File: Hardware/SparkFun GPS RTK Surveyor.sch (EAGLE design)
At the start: 101 parts, among them J16 microSD, J17 Qwiic Right Angle, J3 USB Female Type C Connector, J4 Qwiic Right Angle, J5 USB Female Type C Connector, J6 Start Base, J7 Power Switch, Q2 MBT3904DW1T1, U10 MCP73833, U2 3.3V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

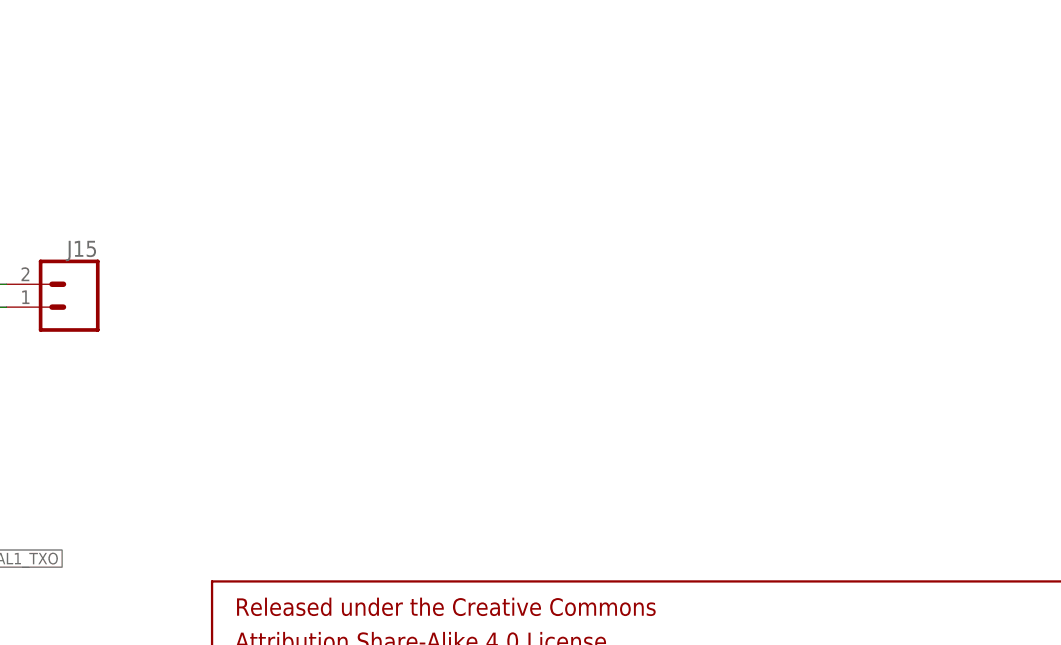
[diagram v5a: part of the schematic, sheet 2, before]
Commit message: Add slide switch to optionally route PPS to Data port
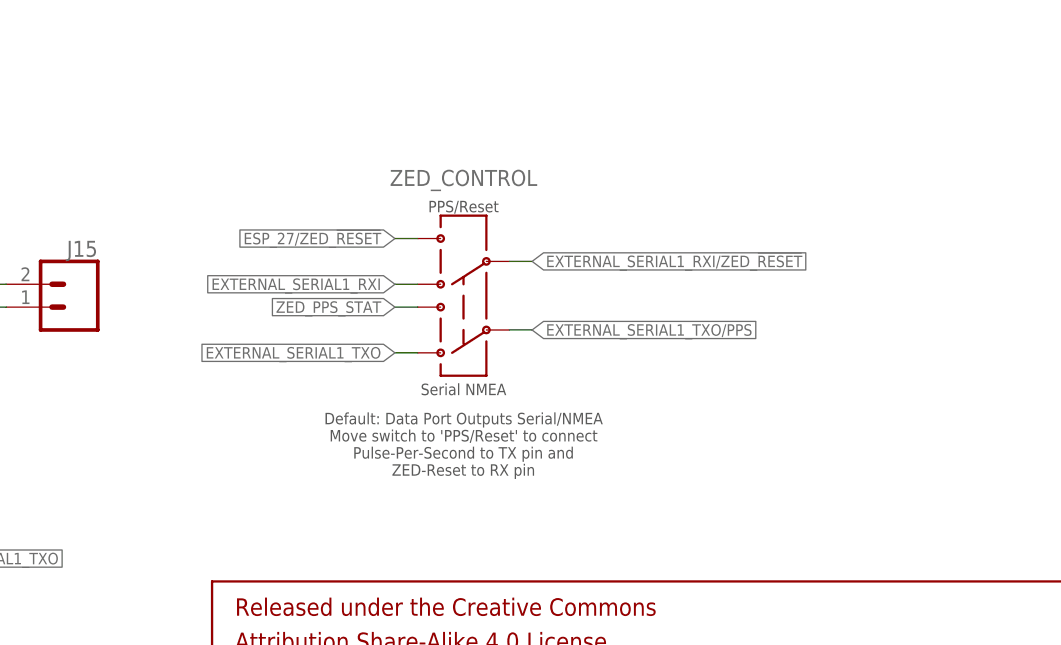
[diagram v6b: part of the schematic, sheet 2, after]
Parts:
- added ZED_CONTROL: (no value), SparkFun-Switches:SWITCH-DPDT-SMD-AYZ0202
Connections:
- new net EXTERNAL_SERIAL1_RXI/ZED_!RESET!: J12.2, J2.3, ZED_CONTROL.5
- new net EXTERNAL_SERIAL1_TXO/PPS: J12.3, J2.2, ZED_CONTROL.2
- net ESP_27/ZED_!RESET!: now also ZED_CONTROL.4
- net EXTERNAL_SERIAL1_RXI: now also ZED_CONTROL.6; no longer J12.2, J2.3
- net EXTERNAL_SERIAL1_TXO: now also ZED_CONTROL.3; no longer J12.3, J2.2
- net ZED_PPS_STAT: now also ZED_CONTROL.1
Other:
- note added: "Default: Data Port Outputs Serial/NMEA Move switch to 'PPS/Reset' to connect Pulse-Per-Second to TX pin and ZED-Reset to RX pin"
- note added: "PPS/Reset"
- note added: "Serial NMEA"

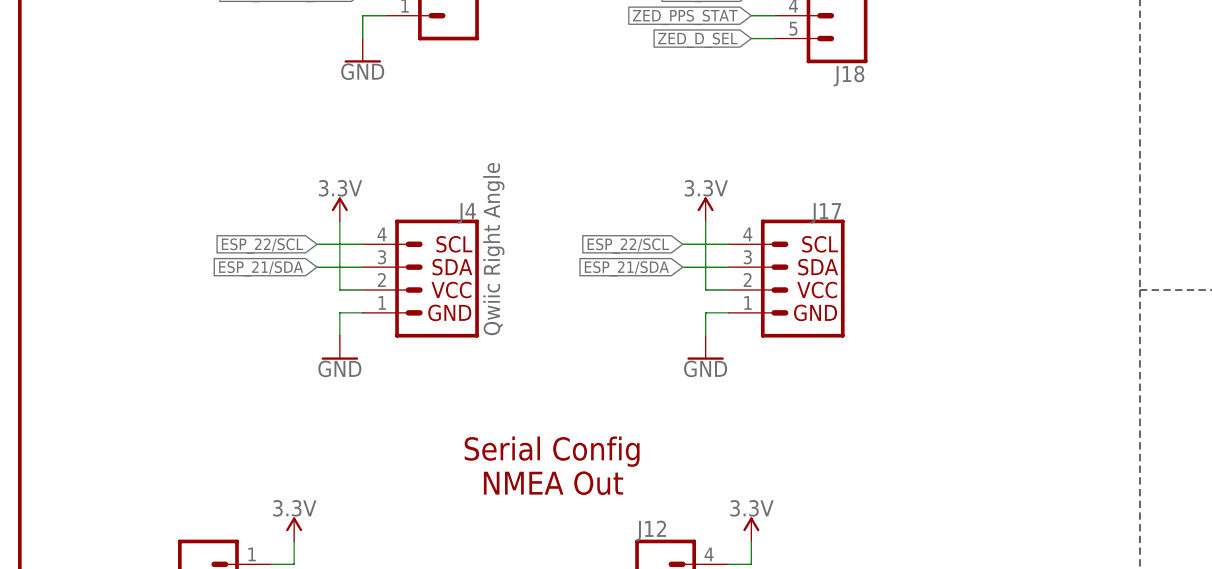
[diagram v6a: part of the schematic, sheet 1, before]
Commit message: Add internal Qwiic connector
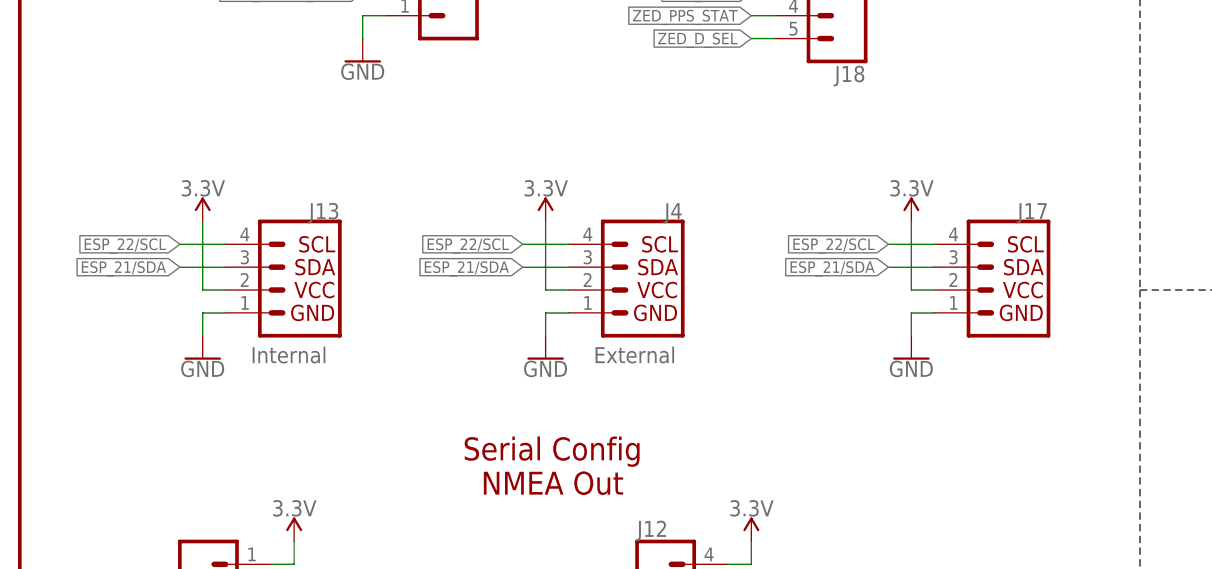
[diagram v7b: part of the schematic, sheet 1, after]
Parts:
- added J13: Internal, SparkFun-Connectors:I2C_STANDARDQWIIC
- J4: value Qwiic Right Angle -> External
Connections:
- net 3.3V: now also J13.2
- net ESP_21/SDA: now also J13.3
- net ESP_22/SCL: now also J13.4
- net GND: now also J13.1
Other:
- moved on the sheet: J17, J4
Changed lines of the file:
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@@
 <part name="JP61" library="SparkFun-Aesthetics" deviceset="FIDUCIAL" device="UFIDUCIAL" value="FIDUCIALUFIDUCIAL"/>
 <part name="SUPPLY8" library="SparkFun-PowerSymbols" deviceset="3.3V" device=""/>
-<part name="J4" library="SparkFun-Connectors" deviceset="I2C_STANDARD" device="QWIIC" value="Qwiic Right Angle"/>
+<part name="J4" library="SparkFun-Connectors" deviceset="I2C_STANDARD" device="QWIIC" value="External"/>
 <part name="LOGO1" library="SparkFun-Aesthetics" deviceset="OSHW-LOGO" device="MINI"/>
 <part name="GND3" library="SparkFun-PowerSymbols" deviceset="GND" device=""/>
@@
 <part name="J18" library="SparkFun-Connectors" deviceset="CONN_05" device="NO_SILK"/>
 <part name="ZED_CONTROL" library="SparkFun-Switches" deviceset="SWITCH-DPDT" device="-SMD-AYZ0202"/>
+<part name="SUPPLY29" library="SparkFun-PowerSymbols" deviceset="3.3V" device=""/>
+<part name="J13" library="SparkFun-Connectors" deviceset="I2C_STANDARD" device="QWIIC" value="Internal"/>
+<part name="GND12" library="SparkFun-PowerSymbols" deviceset="GND" device=""/>
 </parts>
 <sheets>
@@
 <instance part="JP21" gate="G$1" x="416.56" y="33.02" smashed="yes" rot="R270"/>
 <instance part="JP61" gate="G$1" x="419.1" y="33.02" smashed="yes"/>
-<instance part="SUPPLY8" gate="G$1" x="35.56" y="127" smashed="yes">
-<attribute name="VALUE" x="35.56" y="129.794" size="1.778" layer="96" align="bottom-center"/>
-</instance>
-<instance part="J4" gate="G$1" x="45.72" y="119.38" smashed="yes" rot="MR0">
-<attribute name="VALUE" x="51.562" y="133.604" size="1.778" layer="96" font="vector" rot="MR270" align="top-left"/>
-<attribute name="NAME" x="50.8" y="127.254" size="1.778" layer="95" font="vector" rot="MR0"/>
+<instance part="SUPPLY8" gate="G$1" x="58.42" y="127" smashed="yes">
+<attribute name="VALUE" x="58.42" y="129.794" size="1.778" layer="96" align="bottom-center"/>
+</instance>
+<instance part="J4" gate="G$1" x="68.58" y="119.38" smashed="yes" rot="MR0">
+<attribute name="VALUE" x="63.754" y="111.252" size="1.778" layer="96" font="vector" rot="MR180" align="top-left"/>
+<attribute name="NAME" x="73.66" y="127.254" size="1.778" layer="95" font="vector" rot="MR0"/>
 </instance>
 <instance part="LOGO1" gate="G$1" x="417.576" y="45.974" smashed="yes"/>
@@
 <attribute name="REV" x="419.1" y="6.604" size="2.7432" layer="94" font="vector"/>
 </instance>
-<instance part="GND1" gate="1" x="35.56" y="111.76" smashed="yes">
-<attribute name="VALUE" x="35.56" y="111.506" size="1.778" layer="96" align="top-center"/>
+<instance part="GND1" gate="1" x="58.42" y="111.76" smashed="yes">
+<attribute name="VALUE" x="58.42" y="111.506" size="1.778" layer="96" align="top-center"/>
 </instance>
 <instance part="GND28" gate="1" x="304.8" y="208.28" smashed="yes">
@@
 <attribute name="VALUE" x="322.58" y="165.354" size="1.778" layer="96" align="bottom-center"/>
 </instance>
-<instance part="J17" gate="G$1" x="86.36" y="119.38" smashed="yes" rot="MR0">
-<attribute name="NAME" x="91.44" y="127.254" size="1.778" layer="95" font="vector" rot="MR0"/>
-</instance>
-<instance part="GND11" gate="1" x="76.2" y="111.76" smashed="yes">
-<attribute name="VALUE" x="76.2" y="111.506" size="1.778" layer="96" align="top-center"/>
-</instance>
-<instance part="SUPPLY14" gate="G$1" x="76.2" y="127" smashed="yes">
-<attribute name="VALUE" x="76.2" y="129.794" size="1.778" layer="96" align="bottom-center"/>
+<instance part="J17" gate="G$1" x="109.22" y="119.38" smashed="yes" rot="MR0">
+<attribute name="NAME" x="114.3" y="127.254" size="1.778" layer="95" font="vector" rot="MR0"/>
+</instance>
+<instance part="GND11" gate="1" x="99.06" y="111.76" smashed="yes">
+<attribute name="VALUE" x="99.06" y="111.506" size="1.778" layer="96" align="top-center"/>
+</instance>
+<instance part="SUPPLY14" gate="G$1" x="99.06" y="127" smashed="yes">
+<attribute name="VALUE" x="99.06" y="129.794" size="1.778" layer="96" align="bottom-center"/>
 </instance>
 <instance part="J18" gate="G$1" x="91.44" y="152.4" smashed="yes" rot="R180">
 <attribute name="VALUE" x="93.98" y="162.306" size="1.778" layer="96" font="vector" rot="R180"/>
 <attribute name="NAME" x="93.98" y="144.272" size="1.778" layer="95" font="vector" rot="R180"/>
+</instance>
+<instance part="SUPPLY29" gate="G$1" x="20.32" y="127" smashed="yes">
+<attribute name="VALUE" x="20.32" y="129.794" size="1.778" layer="96" align="bottom-center"/>
+</instance>
+<instance part="J13" gate="G$1" x="30.48" y="119.38" smashed="yes" rot="MR0">
+<attribute name="VALUE" x="25.654" y="111.252" size="1.778" layer="96" font="vector" rot="MR180" align="top-left"/>
+<attribute name="NAME" x="35.56" y="127.254" size="1.778" layer="95" font="vector" rot="MR0"/>
+</instance>
+<instance part="GND12" gate="1" x="20.32" y="111.76" smashed="yes">
+<attribute name="VALUE" x="20.32" y="111.506" size="1.778" layer="96" align="top-center"/>
 </instance>
 </instances>
@@
 <segment>
 <pinref part="J4" gate="G$1" pin="2"/>
-<wire x1="38.1" y1="119.38" x2="35.56" y2="119.38" width="0.1524" layer="91"/>
-<wire x1="35.56" y1="119.38" x2="35.56" y2="127" width="0.1524" layer="91"/>
+<wire x1="60.96" y1="119.38" x2="58.42" y2="119.38" width="0.1524" layer="91"/>
+<wire x1="58.42" y1="119.38" x2="58.42" y2="127" width="0.1524" layer="91"/>
 <pinref part="SUPPLY8" gate="G$1" pin="3.3V"/>
 </segment>
@@
 <segment>
 <pinref part="J17" gate="G$1" pin="2"/>
-<wire x1="78.74" y1="119.38" x2="76.2" y2="119.38" width="0.1524" layer="91"/>
-<wire x1="76.2" y1="119.38" x2="76.2" y2="127" width="0.1524" layer="91"/>
+<wire x1="101.6" y1="119.38" x2="99.06" y2="119.38" width="0.1524" layer="91"/>
+<wire x1="99.06" y1="119.38" x2="99.06" y2="127" width="0.1524" layer="91"/>
 <pinref part="SUPPLY14" gate="G$1" pin="3.3V"/>
+</segment>
+<segment>
+<pinref part="J13" gate="G$1" pin="2"/>
+<wire x1="22.86" y1="119.38" x2="20.32" y2="119.38" width="0.1524" layer="91"/>
+<wire x1="20.32" y1="119.38" x2="20.32" y2="127" width="0.1524" layer="91"/>
+<pinref part="SUPPLY29" gate="G$1" pin="3.3V"/>
 </segment>
 </net>
@@
 <segment>
 <pinref part="J4" gate="G$1" pin="1"/>
-<wire x1="38.1" y1="116.84" x2="35.56" y2="116.84" width="0.1524" layer="91"/>
-<wire x1="35.56" y1="116.84" x2="35.56" y2="114.3" width="0.1524" layer="91"/>
+<wire x1="60.96" y1="116.84" x2="58.42" y2="116.84" width="0.1524" layer="91"/>
+<wire x1="58.42" y1="116.84" x2="58.42" y2="114.3" width="0.1524" layer="91"/>
 <pinref part="GND1" gate="1" pin="GND"/>
 </segment>
@@
 <segment>
 <pinref part="J17" gate="G$1" pin="1"/>
-<wire x1="78.74" y1="116.84" x2="76.2" y2="116.84" width="0.1524" layer="91"/>
-<wire x1="76.2" y1="116.84" x2="76.2" y2="114.3" width="0.1524" layer="91"/>
+<wire x1="101.6" y1="116.84" x2="99.06" y2="116.84" width="0.1524" layer="91"/>
+<wire x1="99.06" y1="116.84" x2="99.06" y2="114.3" width="0.1524" layer="91"/>
 <pinref part="GND11" gate="1" pin="GND"/>
+</segment>
+<segment>
+<pinref part="J13" gate="G$1" pin="1"/>
+<wire x1="22.86" y1="116.84" x2="20.32" y2="116.84" width="0.1524" layer="91"/>
+<wire x1="20.32" y1="116.84" x2="20.32" y2="114.3" width="0.1524" layer="91"/>
+<pinref part="GND12" gate="1" pin="GND"/>
 </segment>
 </net>
@@
 <segment>
 <pinref part="J4" gate="G$1" pin="4"/>
-<wire x1="38.1" y1="124.46" x2="33.02" y2="124.46" width="0.1524" layer="91"/>
-<label x="33.02" y="124.46" size="1.27" layer="95" rot="R180" xref="yes"/>
+<wire x1="60.96" y1="124.46" x2="55.88" y2="124.46" width="0.1524" layer="91"/>
+<label x="55.88" y="124.46" size="1.27" layer="95" rot="R180" xref="yes"/>
 </segment>
 <segment>
@@
 <segment>
 <pinref part="J17" gate="G$1" pin="4"/>
-<wire x1="78.74" y1="124.46" x2="73.66" y2="124.46" width="0.1524" layer="91"/>
-<label x="73.66" y="124.46" size="1.27" layer="95" rot="R180" xref="yes"/>
+<wire x1="101.6" y1="124.46" x2="96.52" y2="124.46" width="0.1524" layer="91"/>
+<label x="96.52" y="124.46" size="1.27" layer="95" rot="R180" xref="yes"/>
+</segment>
+<segment>
+<pinref part="J13" gate="G$1" pin="4"/>
+<wire x1="22.86" y1="124.46" x2="17.78" y2="124.46" width="0.1524" layer="91"/>
+<label x="17.78" y="124.46" size="1.27" layer="95" rot="R180" xref="yes"/>
 </segment>
 </net>
@@
 <segment>
 <pinref part="J4" gate="G$1" pin="3"/>
-<wire x1="38.1" y1="121.92" x2="33.02" y2="121.92" width="0.1524" layer="91"/>
-<label x="33.02" y="121.92" size="1.27" layer="95" rot="R180" xref="yes"/>
+<wire x1="60.96" y1="121.92" x2="55.88" y2="121.92" width="0.1524" layer="91"/>
+<label x="55.88" y="121.92" size="1.27" layer="95" rot="R180" xref="yes"/>
 </segment>
 <segment>
@@
 <segment>
 <pinref part="J17" gate="G$1" pin="3"/>
-<wire x1="78.74" y1="121.92" x2="73.66" y2="121.92" width="0.1524" layer="91"/>
-<label x="73.66" y="121.92" size="1.27" layer="95" rot="R180" xref="yes"/>
+<wire x1="101.6" y1="121.92" x2="96.52" y2="121.92" width="0.1524" layer="91"/>
+<label x="96.52" y="121.92" size="1.27" layer="95" rot="R180" xref="yes"/>
+</segment>
+<segment>
+<pinref part="J13" gate="G$1" pin="3"/>
+<wire x1="22.86" y1="121.92" x2="17.78" y2="121.92" width="0.1524" layer="91"/>
+<label x="17.78" y="121.92" size="1.27" layer="95" rot="R180" xref="yes"/>
 </segment>
 </net>

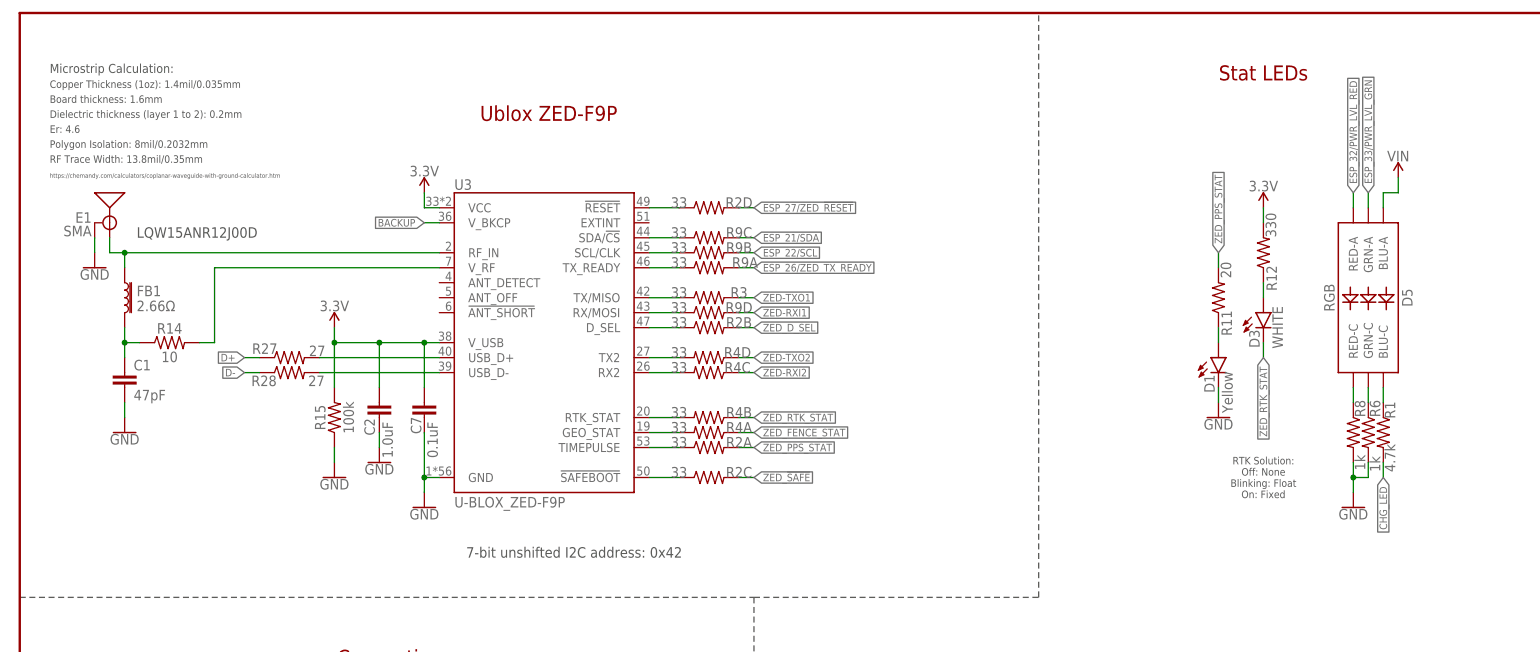
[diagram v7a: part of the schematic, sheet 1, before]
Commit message: v16 hardware: Change out EOL'd LED. Add ESD to RF path.
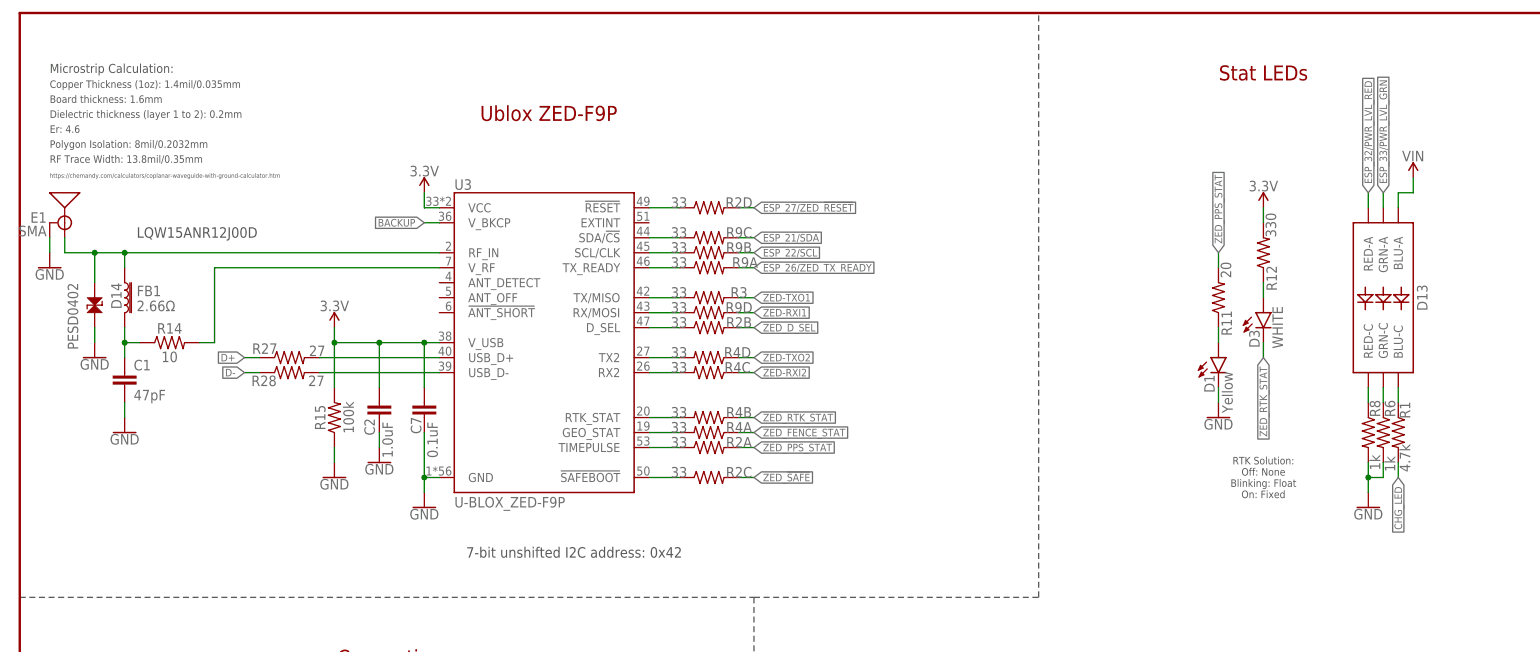
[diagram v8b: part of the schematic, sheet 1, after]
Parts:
- removed D5: RGB, SparkFun-LED:LED-RGBPLCC-6
- added D13: (no value), SparkFun-LED:LED-RGBBRG
- added D14: PESD0402, SparkFun-DiscreteSemi:PESD0402
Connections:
- removed net N$10: D5.GRN-C, R6.1
- removed net N$14: D5.RED-C, R8.1
- removed net N$17: D5.BLU-C, R1.1
- new net N$6: D13.BLU-C, R1.1
- new net N$7: D13.GRN-C, R6.1
- new net N$8: D13.RED-C, R8.1
- net ESP_32/PWR_LVL_RED: now also D13.RED-A; no longer D5.RED-A
- net ESP_33/PWR_LVL_GRN: now also D13.GRN-A; no longer D5.GRN-A
- net GND: now also D14.2
- net GPS_ANT1: now also D14.1
- net VIN: now also D13.BLU-A; no longer D5.BLU-A
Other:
- moved on the sheet: E1, R1, R6, R8
